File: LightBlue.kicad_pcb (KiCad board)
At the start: 4 copper layers, 120 x 120 mm, 262 parts, among them J1 Barrel_Jack, J10 Conn_02x04_Odd_Even, J11 Conn_01x02, J12 Conn_01x02, J13 Bus_M.2_Socket_M, J15 Micro_SD_Card_Det, J16 Conn_02x05_Odd_Even, J2 RJ45_LINK-PP_LPJG0926HENL_Hor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, J3 USB_C_Receptacle_USB2.0, J4 USB_A_Stacked, J5 AudioJack, J6 Conn_01x02, J7 HDMI_A_2.0, J8 SiLabs Mini Debug, J9 Conn_Coaxial, M1 Fan_4pin, Q1 DMP3013SFV-7, Q2 BSZ440N10NS3GATMA1, SW1 SW_USER, SW2 SW_WIPE, T1 PA2467NL, U1 RaspberryPi-CM4Lite, U10 TPD4EUSB30, U11 SiliconLabs-MGM210P, U12 PCM5121PW, U13 TLV74033PDBVR, U14 TPD4EUSB30, U15 TPD4EUSB30, U16 BD9D321EFJ, U17 BD9D321EFJ, U18 74LVC1G07, U19 74LVC1G07, U20 LP5569RTWR, U21 PCF85063AT, U22 RT9742GGJ5, U23 TPS23734, U24 TCMT1107, U4 CP2102N-Axx-xQFN20, U5 FSUSB42MUX, U6 FSUSB42MUX, U7 USB2422, U8 TPD4EUSB30, U9 AP2171W, Y1 24MHz, Y2 X32K768S301

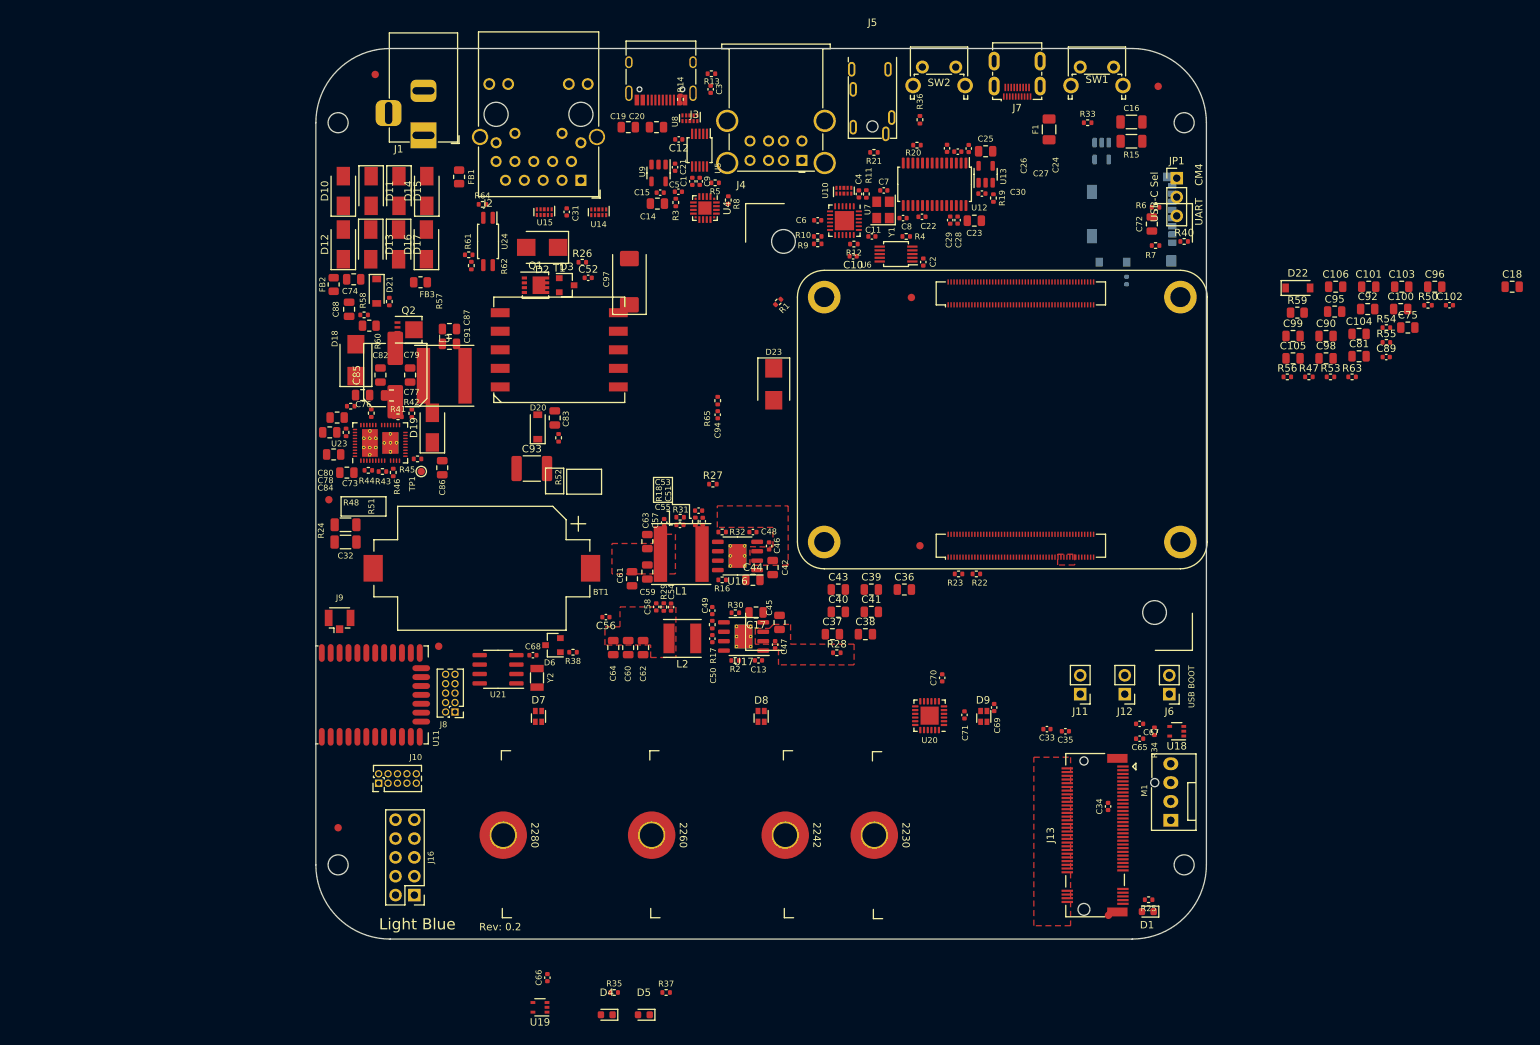
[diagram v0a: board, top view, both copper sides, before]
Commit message: Change button length and start layouting
Change the length and positioning of the buttons and start layouting a
bit. Move components where needed.

Signed-off-by: Stefan Agner <stefan@agner.ch>
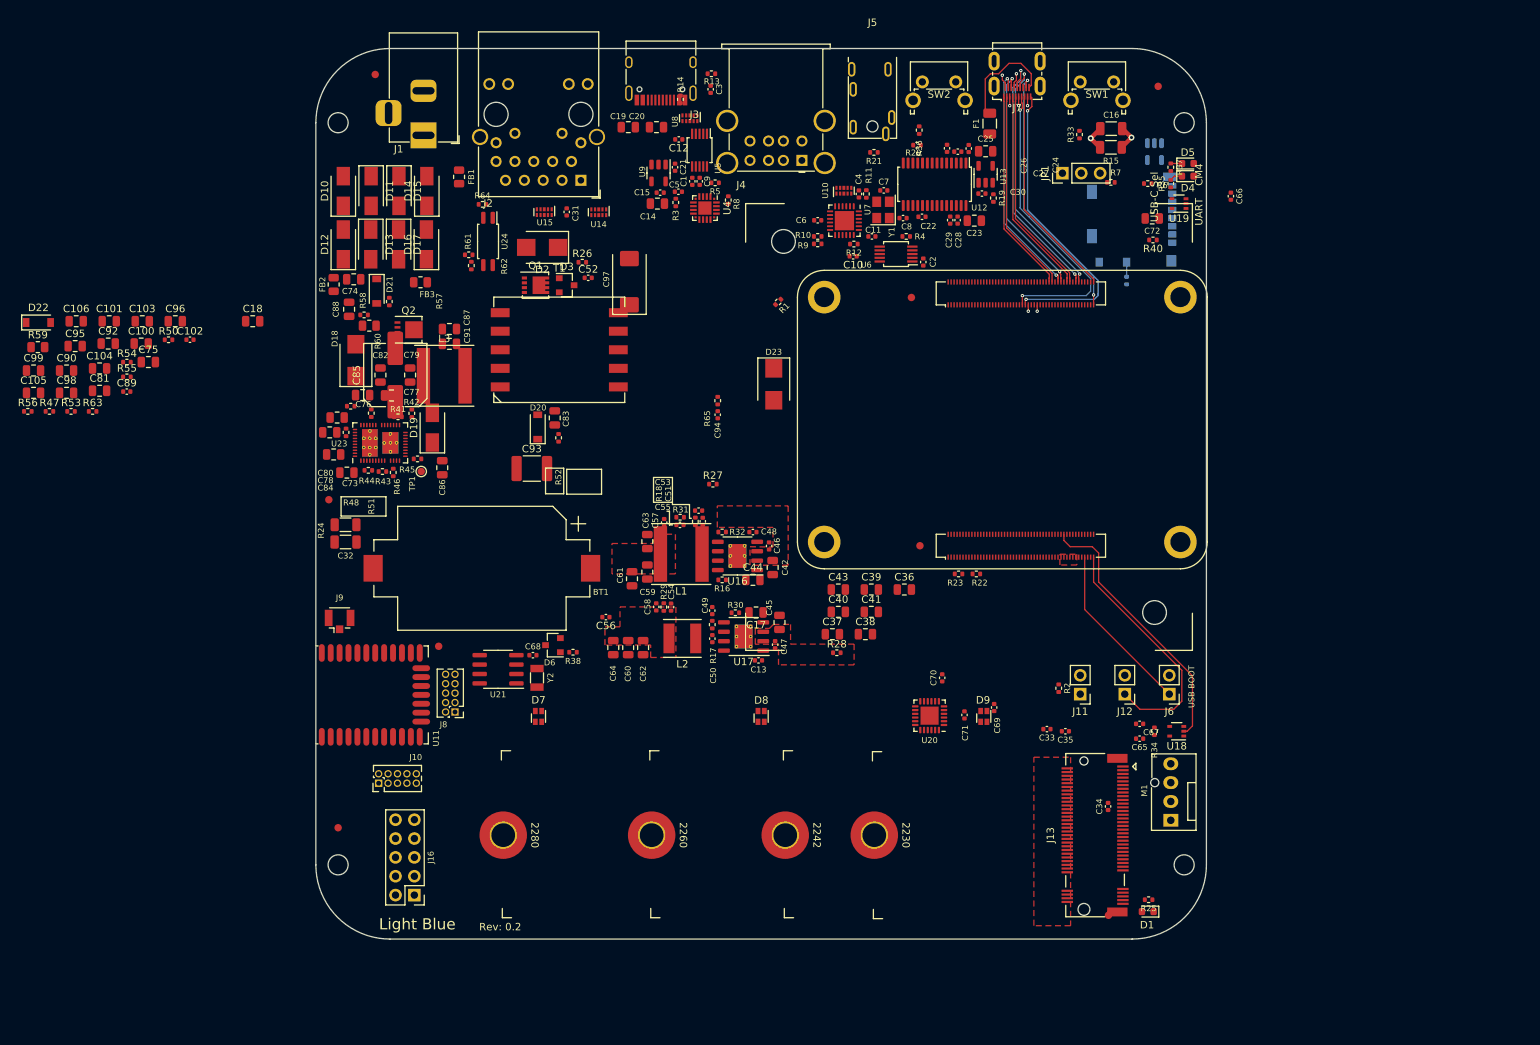
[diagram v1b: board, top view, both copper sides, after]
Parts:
- SW1: footprint Button_Switch_THT:SW_Tactile_SPST_Angled_PTS645Vx58-2LFS -> Button_Switch_THT:SW_Tactile_SPST_Angled_PTS645Vx83-2LFS
- SW2: footprint Button_Switch_THT:SW_Tactile_SPST_Angled_PTS645Vx39-2LFS -> Button_Switch_THT:SW_Tactile_SPST_Angled_PTS645Vx58-2LFS
- moved C100 169.8 mm to (6.47, 69.8)
- moved C101 169.8 mm to (2.16, 66.8)
- moved C102 169.8 mm to (13.0, 69.2)
- moved C90 169.8 mm to (-3.59, 73.4)
- moved C95 169.8 mm to (-2.43, 70.1)
- moved C96 169.8 mm to (11.1, 66.8)
- moved C98 169.8 mm to (-3.59, 76.4)
- moved R47 169.8 mm to (-5.90, 78.9)
- moved R50 169.8 mm to (10.2, 69.2)
- moved R53 169.8 mm to (-2.99, 78.9)
- moved R54 169.8 mm to (4.54, 72.3)
- moved R55 169.8 mm to (4.54, 74.2)
- moved R56 169.8 mm to (-8.81, 78.9)
- moved R59 169.8 mm to (-7.46, 70.2)
- moved R63 169.8 mm to (-0.08, 78.9)
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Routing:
- net /CM4/HDMI.HPD: track 0.00 -> 41.8 mm, vias 0 -> 2
- net /CM4/HDMI.CEC: track 0.00 -> 41.0 mm, vias 0 -> 2
- net /CM4/~FAN_PWM: track 0.00 -> 36.2 mm
- net /CM4/HDMI.SDA: track 0.00 -> 35.5 mm, vias 0 -> 2
- net /CM4/HDMI.CLK+: track 0.00 -> 34.9 mm, vias 0 -> 2
- net /CM4/HDMI.CLK-: track 0.00 -> 34.2 mm, vias 0 -> 2
- net /CM4/GLOBAL_EN: track 0.00 -> 33.3 mm
- net /CM4/HDMI.D1-: track 0.00 -> 32.0 mm, vias 0 -> 2
- net /CM4/HDMI.D1+: track 0.00 -> 32.0 mm, vias 0 -> 2
- net /CM4/HDMI.SCL: track 0.00 -> 28.9 mm
- net /CM4/HDMI.D0+: track 0.00 -> 28.0 mm
- net /CM4/HDMI.D0-: track 0.00 -> 28.0 mm
- net /CM4/HDMI.D2-: track 0.00 -> 27.5 mm
- net /CM4/HDMI.D2+: track 0.00 -> 27.5 mm
- net /Ethernet/ETH_SHLD: track 0.00 -> 27.0 mm
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
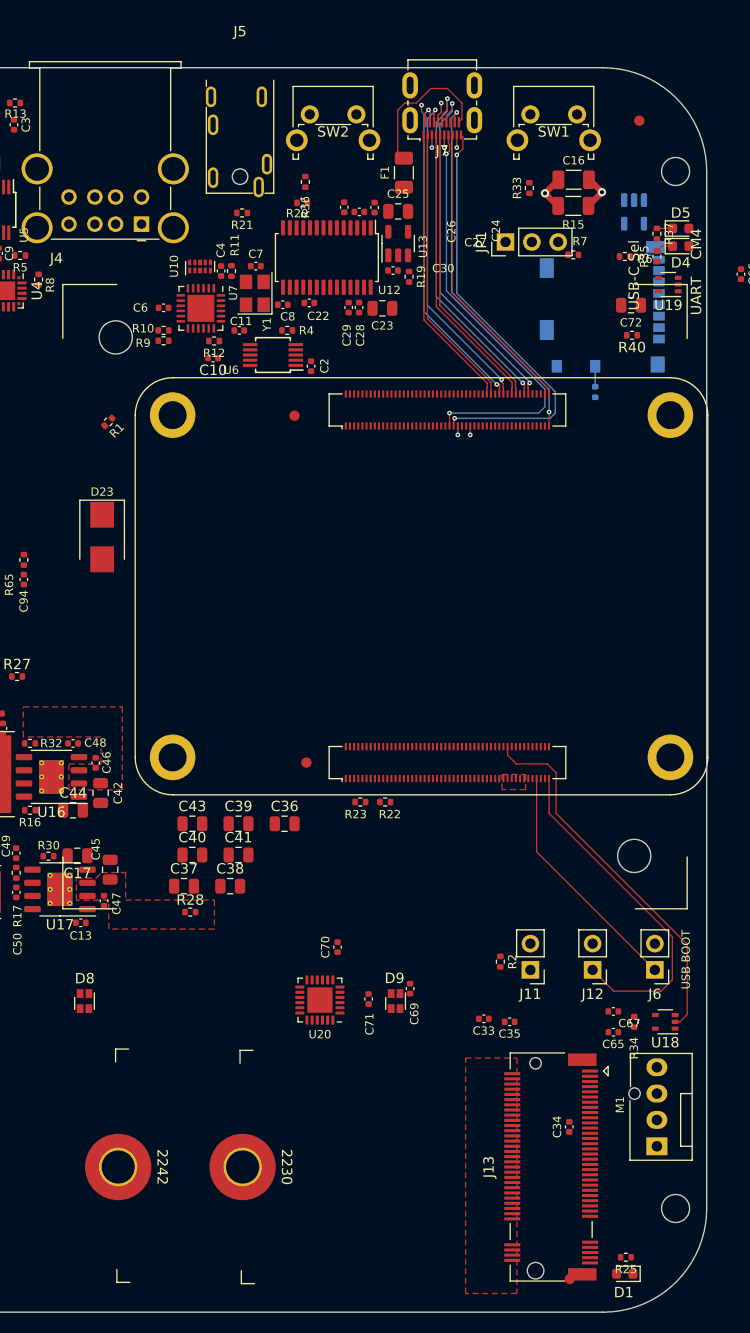
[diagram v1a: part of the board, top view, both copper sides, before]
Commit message: Use impedance for JLC7628 stackup/switch HDMI/SW2 placement
Use JLC7628 impedance values to get more options in color selection.
Also this leads to slightly wider traces typically, and it will be
easier to switch back to JLC2313 or the like than the other way around.

Also swap placing of HDMI/SW2 and rotate the heatsink by 90° for easier
routing.

Signed-off-by: Stefan Agner <stefan@agner.ch>
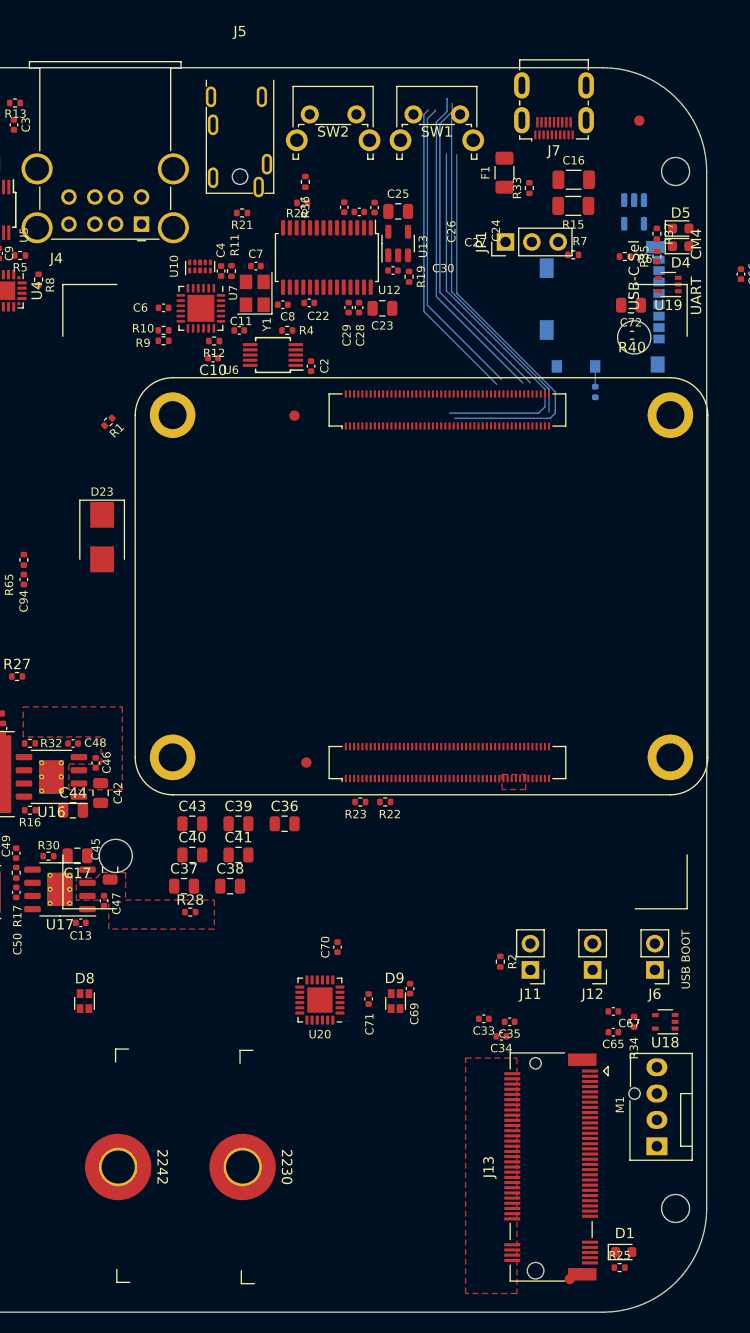
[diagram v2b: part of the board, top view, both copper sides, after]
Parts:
- moved SW1 11.3 mm to (121.7, 34.5)
- moved C34 10.9 mm to (130.2, 123.4), turned to 180 degrees
- moved J7 10.8 mm to (135.3, 31.7)
- moved F1 9.70 mm to (130.5, 40.1)
- moved D1 2.10 mm to (142.0, 144.2), turned to 0 degrees
- moved R25 1.17 mm to (141.6, 145.7), turned to 0 degrees
- turned HS1 to 90 degrees
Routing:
- net /CM4/~SW_USER: track 0.00 -> 58.8 mm
- net GND: track 13.1 -> 64.2 mm, vias 8 -> 0
- net /CM4/~FAN_PWM: track 36.2 -> 0.00 mm
- net /CM4/HDMI.SDA: track 35.5 -> 0.00 mm, vias 2 -> 0
- net /CM4/HDMI.CLK-: track 34.2 -> 0.00 mm, vias 2 -> 0
- net /CM4/GLOBAL_EN: track 33.3 -> 0.00 mm
- net /CM4/HDMI.D1-: track 32.0 -> 0.00 mm, vias 2 -> 0
- net /CM4/HDMI.D1+: track 32.0 -> 0.00 mm, vias 2 -> 0
- net /CM4/HDMI.SCL: track 28.9 -> 0.00 mm
- net /CM4/HDMI.D0+: track 28.0 -> 0.00 mm
- net /CM4/HDMI.D0-: track 28.0 -> 0.00 mm
- net /CM4/HDMI.D2-: track 27.5 -> 0.00 mm
- net /CM4/HDMI.D2+: track 27.5 -> 0.00 mm
- net /CM4/~RPI_BOOT: track 23.2 -> 0.00 mm
- net Net-(F1-Pad2): track 14.5 -> 0.00 mm
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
